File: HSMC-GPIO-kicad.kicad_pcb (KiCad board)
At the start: 2 copper layers, 88.9 x 78.1 mm, 93 parts, among them J1 HSMC, J2 Conn_01x03_Male, J3 I2C, J4 Screw_Terminal_01x04, J5 Conn_02x20_Odd_Even, U1 MC78M05_TO252, U2 TCA9517

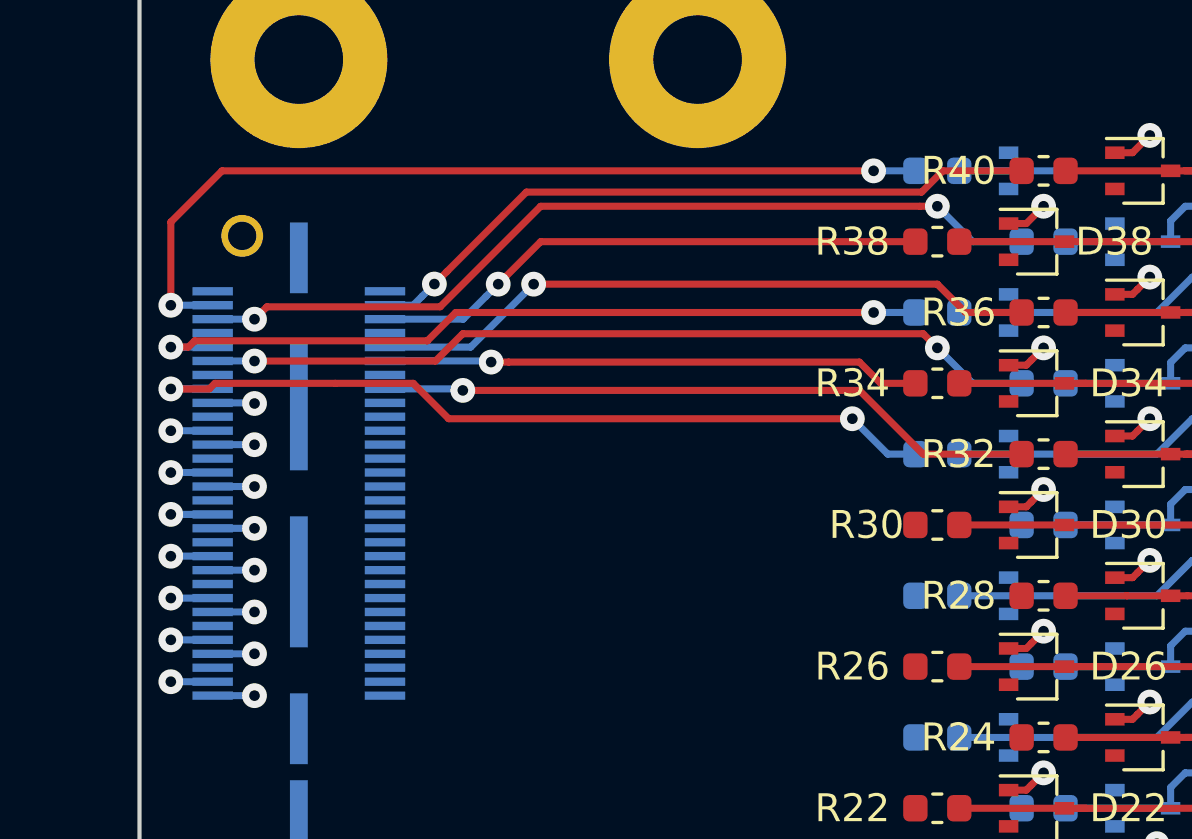
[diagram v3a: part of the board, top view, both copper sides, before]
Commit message: Continue routing GPIO ribbon connector
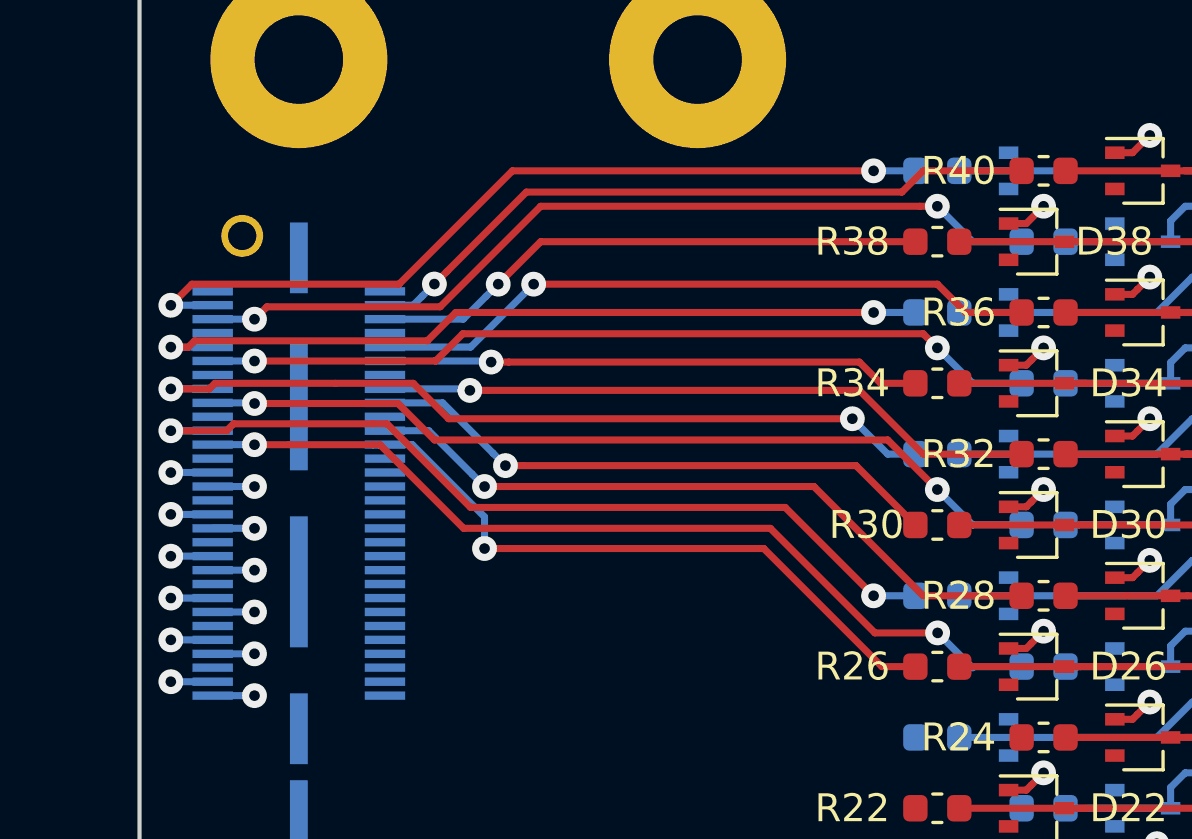
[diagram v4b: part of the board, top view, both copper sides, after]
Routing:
- net /GPIO24: track 1.50 -> 32.3 mm, vias 1 -> 2
- net /GPIO26: track 1.50 -> 30.9 mm, vias 1 -> 2
- net /GPIO28: track 1.51 -> 30.8 mm, vias 1 -> 2
- net /GPIO27: track 0.00 -> 25.3 mm, vias 0 -> 1
- net /GPIO25: track 0.00 -> 23.0 mm, vias 0 -> 1
- net /GPIO29: track 0.00 -> 20.8 mm, vias 0 -> 1
- net /GPIO38: track 31.9 -> 30.2 mm

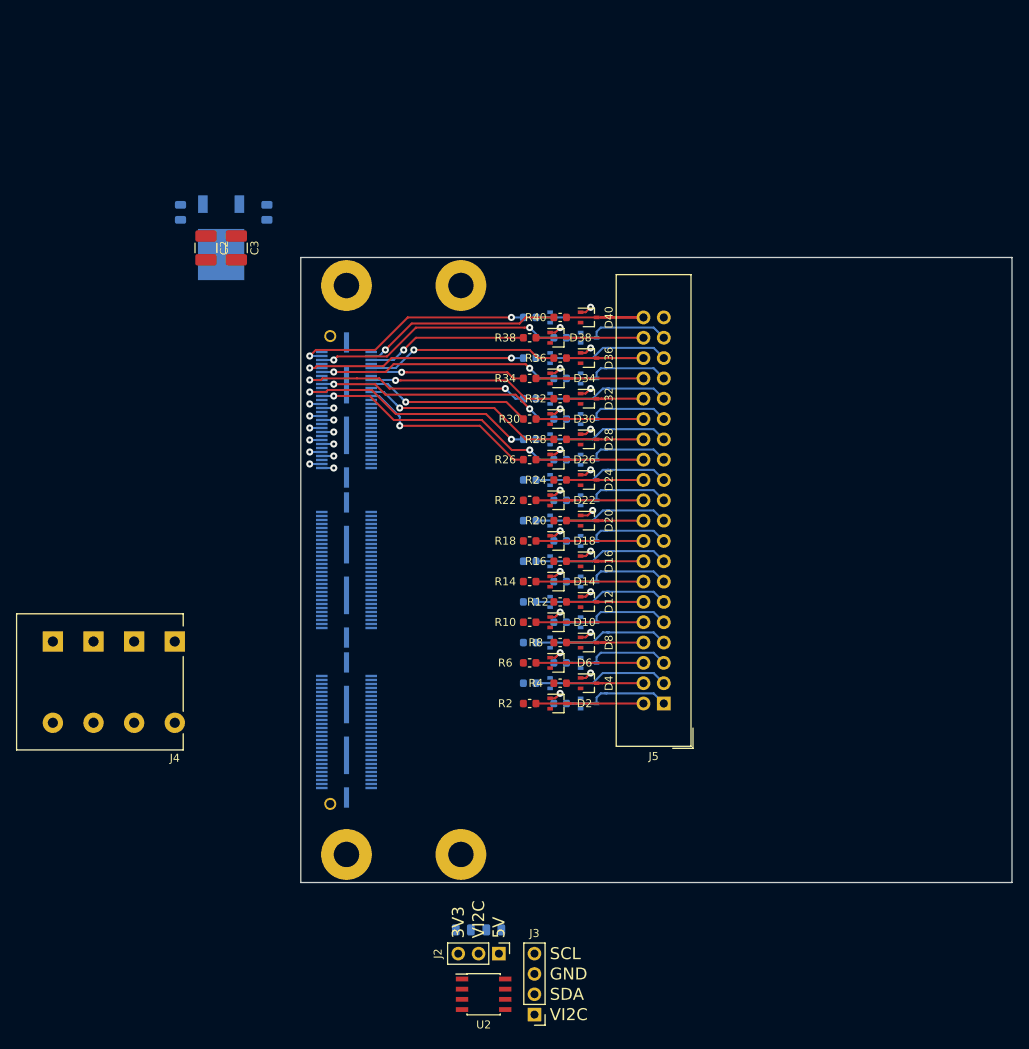
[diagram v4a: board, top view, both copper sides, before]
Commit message: Finish routing GPIO port
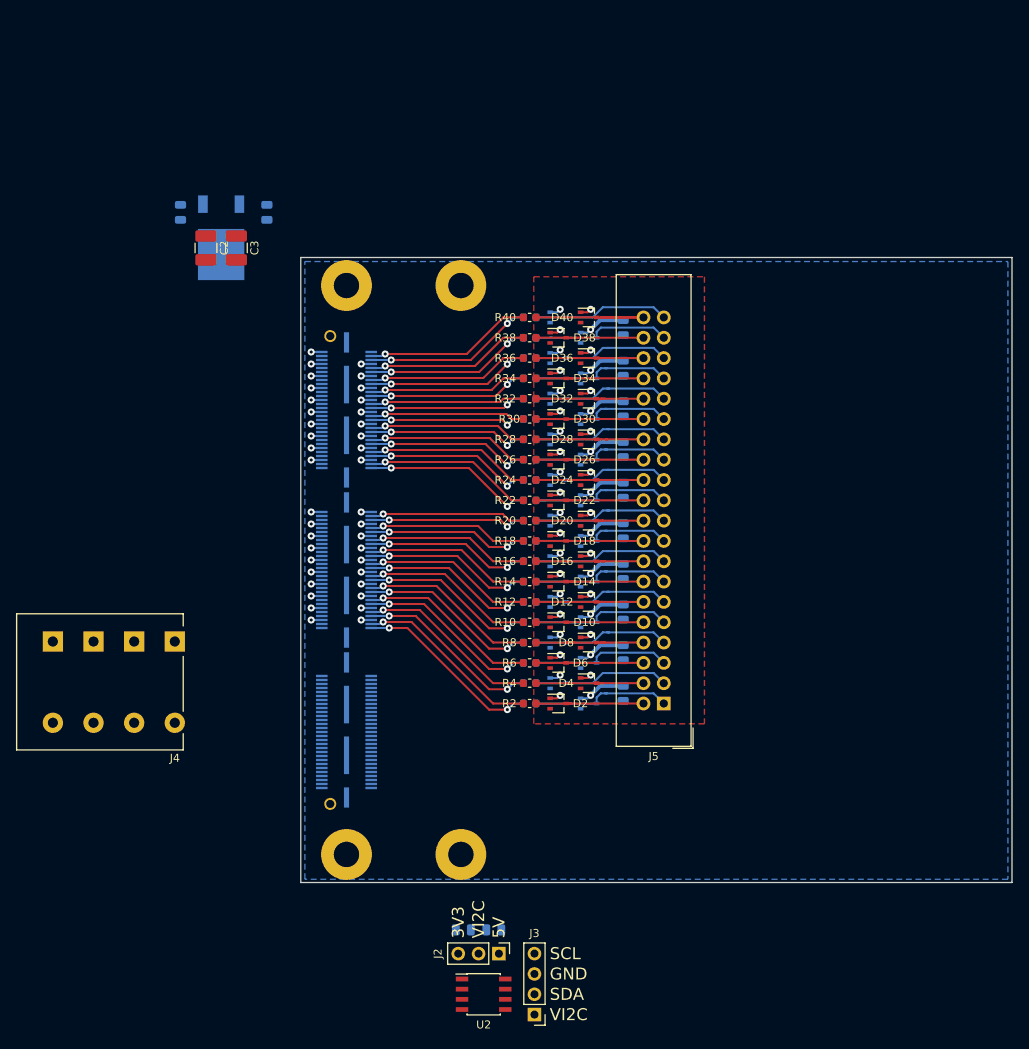
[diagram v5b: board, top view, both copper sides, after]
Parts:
- added C10: 100n, Capacitor_SMD:C_0805_2012Metric, B.Cu at (65.7, 64.6)
- added C11: 100n, Capacitor_SMD:C_0805_2012Metric, B.Cu at (65.7, 59.6)
- added C12: 100n, Capacitor_SMD:C_0805_2012Metric, B.Cu at (65.7, 54.5)
- added C13: 100n, Capacitor_SMD:C_0805_2012Metric, B.Cu at (65.7, 49.4)
- added C14: 100n, Capacitor_SMD:C_0805_2012Metric, B.Cu at (65.7, 44.3)
- added C15: 100n, Capacitor_SMD:C_0805_2012Metric, B.Cu at (65.7, 39.2)
- added C16: 100n, Capacitor_SMD:C_0805_2012Metric, B.Cu at (65.7, 34.2)
- added C7: 100n, Capacitor_SMD:C_0805_2012Metric, B.Cu at (65.7, 79.9)
- added C8: 100n, Capacitor_SMD:C_0805_2012Metric, B.Cu at (65.7, 74.8)
- added C9: 100n, Capacitor_SMD:C_0805_2012Metric, B.Cu at (65.7, 69.7)
- moved R1 3.81 mm to (54.0, 81.2)
- moved R12 3.81 mm to (54.0, 68.5)
- moved R13 3.81 mm to (54.0, 65.9)
- moved R16 3.81 mm to (54.0, 63.4)
- moved R17 3.81 mm to (54.0, 60.8)
- moved R20 3.81 mm to (54.0, 58.3)
- moved R21 3.81 mm to (54.0, 55.8)
- moved R24 3.81 mm to (54.0, 53.2)
- moved R25 3.81 mm to (54.0, 50.7)
- moved R28 3.81 mm to (54.0, 48.1)
- moved R29 3.81 mm to (54.0, 45.6)
- moved R32 3.81 mm to (54.0, 43.1)
- moved R33 3.81 mm to (54.0, 40.5)
- moved R36 3.81 mm to (54.0, 38.0)
- moved R37 3.81 mm to (54.0, 35.4)
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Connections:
- J1 pad 101: /GPIO0 -> Net-(J1-Pad101)
- J1 pad 102: /GPIO1 -> /GPIO20
- J1 pad 103: /GPIO2 -> Net-(J1-Pad103)
- J1 pad 104: /GPIO3 -> /GPIO21
- J1 pad 107: /GPIO4 -> Net-(J1-Pad107)
- J1 pad 108: /GPIO5 -> /GPIO22
- J1 pad 109: /GPIO6 -> Net-(J1-Pad109)
- J1 pad 110: /GPIO7 -> /GPIO23
- J1 pad 113: /GPIO8 -> Net-(J1-Pad113)
- J1 pad 114: /GPIO9 -> /GPIO24
- J1 pad 115: /GPIO10 -> Net-(J1-Pad115)
- J1 pad 116: /GPIO11 -> /GPIO25
- J1 pad 119: /GPIO12 -> Net-(J1-Pad119)
- J1 pad 120: /GPIO13 -> /GPIO26
- J1 pad 121: /GPIO14 -> Net-(J1-Pad121)
- J1 pad 122: /GPIO15 -> /GPIO27
- J1 pad 125: /GPIO16 -> Net-(J1-Pad125)
- J1 pad 126: /GPIO17 -> /GPIO28
- J1 pad 127: /GPIO18 -> Net-(J1-Pad127)
- J1 pad 128: /GPIO19 -> /GPIO29
- J1 pad 131: /GPIO20 -> Net-(J1-Pad131)
- J1 pad 132: /GPIO21 -> /GPIO30
- J1 pad 133: /GPIO22 -> Net-(J1-Pad133)
- J1 pad 134: /GPIO23 -> /GPIO31
- J1 pad 137: /GPIO24 -> Net-(J1-Pad137)
- J1 pad 138: /GPIO25 -> /GPIO32
- J1 pad 139: /GPIO26 -> Net-(J1-Pad139)
- J1 pad 140: /GPIO27 -> /GPIO33
- J1 pad 143: /GPIO28 -> Net-(J1-Pad143)
- J1 pad 144: /GPIO29 -> /GPIO34
- J1 pad 145: /GPIO30 -> Net-(J1-Pad145)
- J1 pad 146: /GPIO31 -> /GPIO35
- J1 pad 149: /GPIO32 -> Net-(J1-Pad149)
- J1 pad 150: /GPIO33 -> /GPIO36
- J1 pad 151: /GPIO34 -> Net-(J1-Pad151)
- J1 pad 152: /GPIO35 -> /GPIO37
- J1 pad 155: /GPIO36 -> Net-(J1-Pad155)
- J1 pad 156: /GPIO37 -> /GPIO38
- J1 pad 157: /GPIO38 -> Net-(J1-Pad157)
- J1 pad 42: Net-(J1-Pad42) -> /GPIO0
- J1 pad 44: Net-(J1-Pad44) -> /GPIO1
- J1 pad 48: Net-(J1-Pad48) -> /GPIO2
- J1 pad 50: Net-(J1-Pad50) -> /GPIO3
- J1 pad 54: Net-(J1-Pad54) -> /GPIO4
- J1 pad 56: Net-(J1-Pad56) -> /GPIO5
- J1 pad 60: Net-(J1-Pad60) -> /GPIO6
- J1 pad 62: Net-(J1-Pad62) -> /GPIO7
- J1 pad 66: Net-(J1-Pad66) -> /GPIO8
- J1 pad 68: Net-(J1-Pad68) -> /GPIO9
- J1 pad 72: Net-(J1-Pad72) -> /GPIO10
- J1 pad 74: Net-(J1-Pad74) -> /GPIO11
- J1 pad 78: Net-(J1-Pad78) -> /GPIO12
- J1 pad 80: Net-(J1-Pad80) -> /GPIO13
- J1 pad 84: Net-(J1-Pad84) -> /GPIO14
- J1 pad 86: Net-(J1-Pad86) -> /GPIO15
- J1 pad 90: Net-(J1-Pad90) -> /GPIO16
- J1 pad 92: Net-(J1-Pad92) -> /GPIO17
- J1 pad 96: Net-(J1-Pad96) -> /GPIO18
- J1 pad 98: Net-(J1-Pad98) -> /GPIO19
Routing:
- net +3V3: track 0.00 -> 100.1 mm, vias 0 -> 40
- net +12V: track 0.00 -> 23.8 mm, vias 0 -> 19
- net /GPIO1: track 0.00 -> 23.3 mm, vias 0 -> 1
- net /GPIO3: track 0.00 -> 22.9 mm, vias 0 -> 1
- net /GPIO5: track 0.00 -> 22.5 mm, vias 0 -> 1
- net /GPIO0: track 1.50 -> 23.6 mm, vias 1 -> 2
- net /GPIO7: track 0.00 -> 21.8 mm, vias 0 -> 1
- net /GPIO2: track 1.50 -> 23.1 mm, vias 1 -> 2
- net /GPIO9: track 0.00 -> 21.6 mm, vias 0 -> 1
- net /GPIO4: track 1.50 -> 22.7 mm, vias 1 -> 2
- net /GPIO11: track 0.00 -> 21.2 mm, vias 0 -> 1
- net /GPIO21: track 0.00 -> 21.1 mm, vias 0 -> 1
- net /GPIO6: track 1.50 -> 22.3 mm, vias 1 -> 2
- net /GPIO13: track 0.00 -> 20.8 mm, vias 0 -> 1
- net /GPIO23: track 0.00 -> 20.7 mm, vias 0 -> 1
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- added copper zone on F.Cu, net +3V3
- added copper zone on B.Cu, net GND
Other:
- net class Logic_SE50 removed
- net class Power: trace_width 2.54 -> 0.508

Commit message: Adjust board and plane sizes
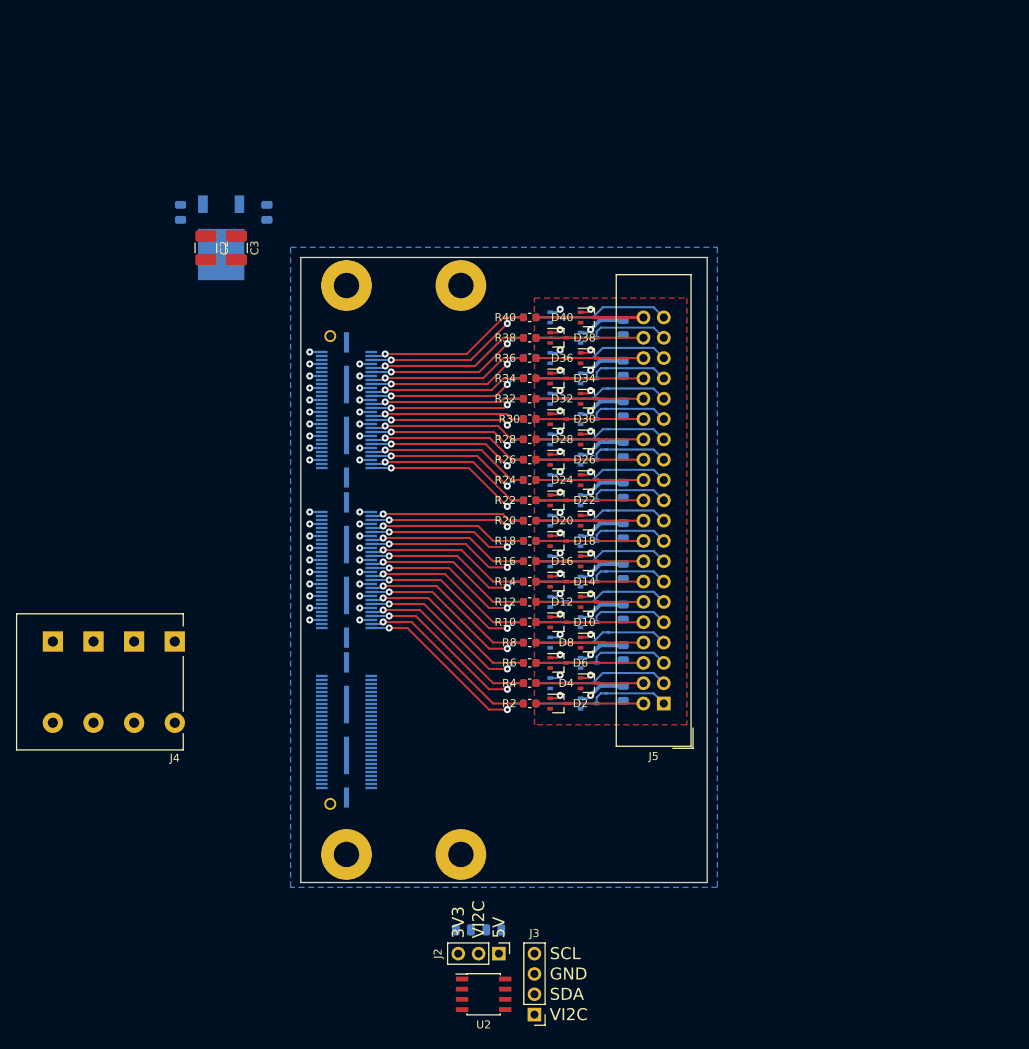
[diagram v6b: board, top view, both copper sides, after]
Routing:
- net +3V3: track 100.1 -> 103.7 mm
- net +12V: track 23.8 -> 27.2 mm
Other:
- board size 88.9 x 78.1 mm -> 50.8 x 78.1 mm

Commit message: Finish initial placement and routing
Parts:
- removed C1: 100n, Capacitor_SMD:C_0805_2012Metric
- added C18: 10u, Capacitor_Tantalum_SMD:CP_EIA-3528-21_Kemet-B, B.Cu at (62.9, 34.6)
- added C19: 10u, Capacitor_Tantalum_SMD:CP_EIA-3528-21_Kemet-B, B.Cu at (68.0, 34.6)
- added C20: 10u, Capacitor_Tantalum_SMD:CP_EIA-3528-21_Kemet-B, B.Cu at (57.9, 34.6)
- added MH1: MountingHole, HSMC:MountingHole, F.Cu at (85.1, 100.0)
- added MH2: MountingHole, HSMC:MountingHole, F.Cu at (85.1, 28.9)
- C2, C3: footprint Capacitor_SMD:C_1210_3225Metric_Pad1.42x2.65mm_HandSolder -> Capacitor_Tantalum_SMD:CP_EIA-3528-21_Kemet-B
- C4, U1: moved to F.Cu
- J1: moved to B.Cu
- J4: footprint Phoenix_MFKDS:Phoenix_MFKDS-5.08_1x04_P5.08mm -> TerminalBlock:TerminalBlock_bornier-4_P5.08mm
- moved J4 83.4 mm to (73.1, 29.4)
- moved C4 75.0 mm to (46.4, 90.4), turned to 0 degrees
- moved C3 69.3 mm to (42.2, 88.9)
- moved U1 67.2 mm to (46.1, 82.8), turned to 0 degrees
- moved C2 60.5 mm to (44.2, 76.4), turned to 0 degrees
- moved J2 21.2 mm to (58.7, 93.0)
- moved U2 21.2 mm to (56.8, 98.1)
- moved J3 21.1 mm to (62.8, 100.6)
- moved C5 16.2 mm to (58.8, 96.1), turned to 90 degrees
- moved D1 15.6 mm to (75.1, 88.5)
- moved D12 15.6 mm to (75.1, 75.8)
- moved D16 15.6 mm to (75.1, 70.7)
- moved D20 15.6 mm to (75.1, 65.6)
- moved D25 15.6 mm to (75.1, 58.0)
- moved D28 15.6 mm to (75.1, 55.5)
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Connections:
- J4 pad 1: +12V -> GND
- J4 pad 2: +5V -> +12V
- J4 pad 3: +3V3 -> +5V
- J4 pad 4: GND -> +3V3
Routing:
- net GND: track 28.1 -> 149.9 mm, vias 20 -> 51
- net +3V3: track 103.7 -> 225.2 mm
- net +5V: track 0.00 -> 120.8 mm
- net +12V: track 27.2 -> 118.8 mm
- net /SDA: track 0.00 -> 38.3 mm, vias 0 -> 1
- net /SCL: track 0.00 -> 32.8 mm, vias 0 -> 1
- net /GPIO19: track 19.5 -> 37.8 mm
- net /GPIO21: track 21.1 -> 39.3 mm
- net /GPIO28: track 19.6 -> 37.5 mm
- net /GPIO26: track 20.0 -> 37.8 mm
- net /GPIO12: track 21.0 -> 38.7 mm
- net /GPIO24: track 20.5 -> 38.2 mm
- net /GPIO17: track 19.9 -> 37.6 mm
- net /GPIO13: track 20.8 -> 38.5 mm
- net /GPIO11: track 21.2 -> 38.9 mm
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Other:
- board size 50.8 x 78.1 mm -> 63.5 x 78.1 mm
- board text added: "12V"
- board text added: "3.3V"
- board text added: "HSMC-GPIO v1.0 Caleb Reister"
- board text removed: "3V3"

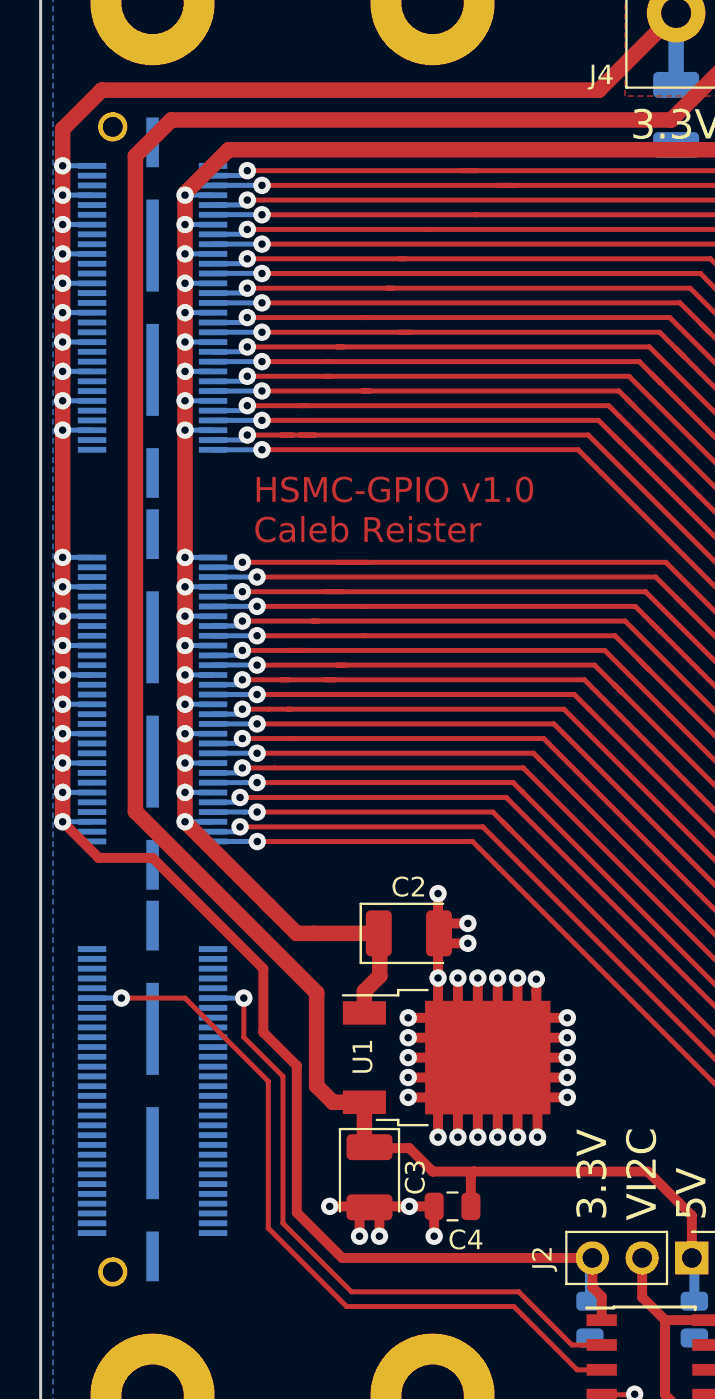
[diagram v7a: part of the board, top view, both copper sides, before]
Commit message: Fix major error in HSMC footprints
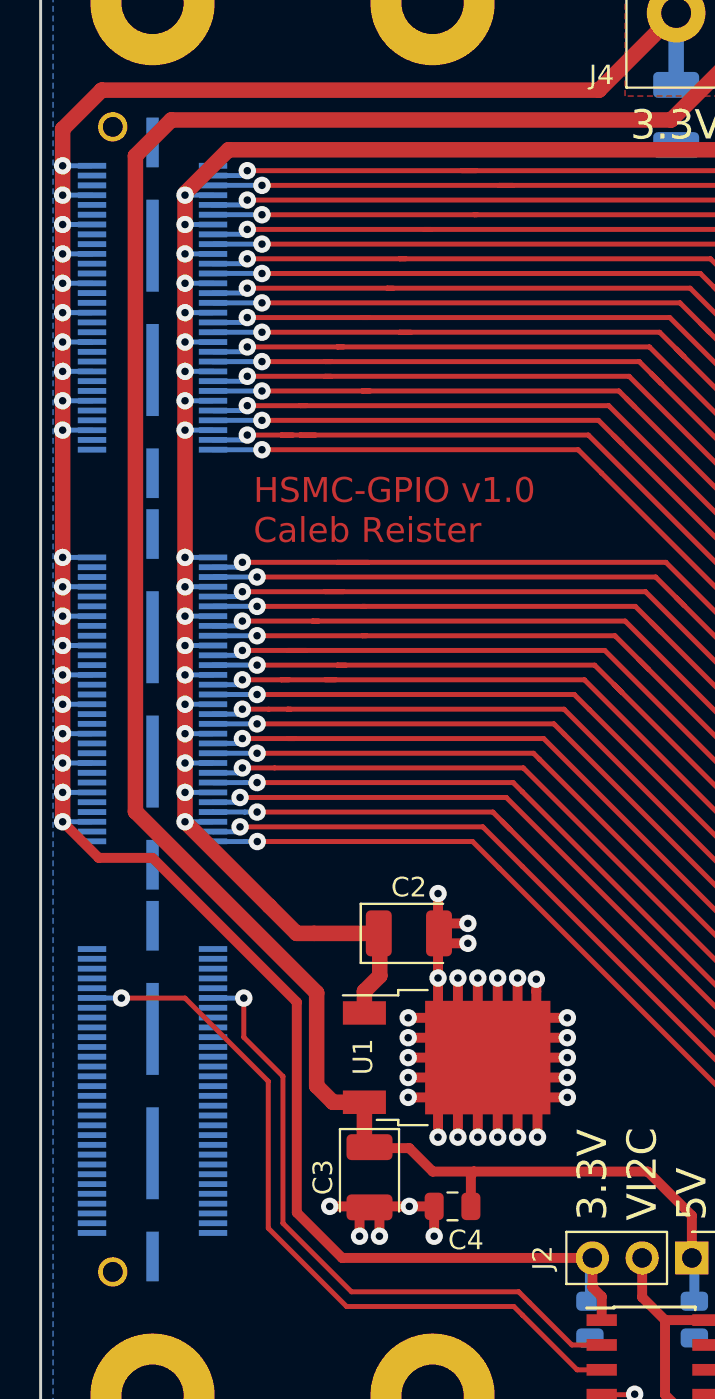
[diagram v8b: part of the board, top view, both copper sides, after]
